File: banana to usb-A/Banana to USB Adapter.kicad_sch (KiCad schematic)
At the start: 11 parts, among them J1 USB_A, J2 Positive, J3 Negative, J4 Data

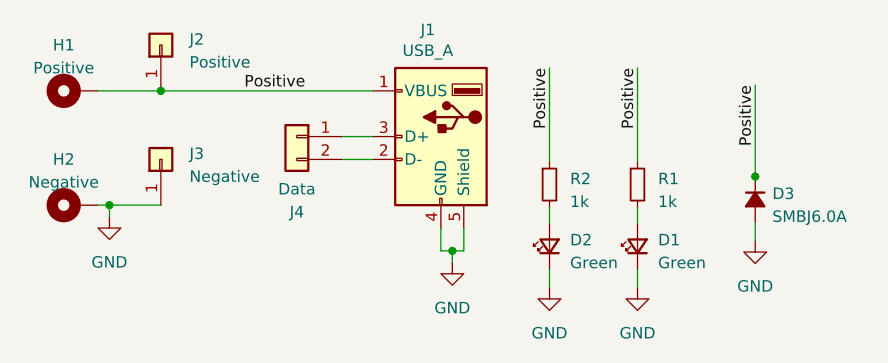
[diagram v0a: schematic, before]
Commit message: No design changes to PCB. Removed extra LED reference in schematic, changed TVS diode to D2, and uploaded PCB.
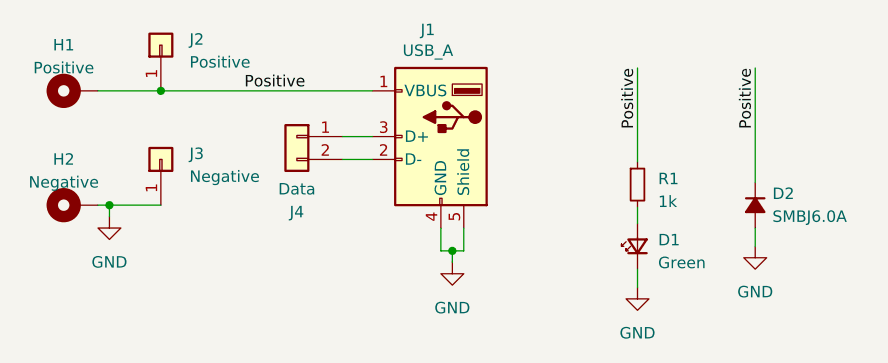
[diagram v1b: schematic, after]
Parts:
- removed D2: Green, LED_SMD:LED_1206_3216Metric_Pad1.42x1.75mm_HandSolder, symbol Device:LED_Small
- removed R2: 1k, Resistor_SMD:R_1206_3216Metric_Pad1.30x1.75mm_HandSolder, symbol Device:R_Small
- renumbered D3 to D2
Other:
- moved on the sheet: D2
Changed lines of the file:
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@@
     (company "baldengineer.com")
   )
-  (junction (at 241.935 86.995) (diameter 0) (color 0 0 0 0)
-  )
   (junction (at 208.28 95.25) (diameter 0) (color 0 0 0 0)
   )
@@
     (stroke (width 0) (type default))
   )
-  (wire (pts (xy 241.935 76.835) (xy 241.935 86.995))
+  (wire (pts (xy 241.935 74.93) (xy 241.935 87.63))
     (stroke (width 0) (type default))
   )
@@
     (stroke (width 0) (type default))
   )
-  (wire (pts (xy 219.075 97.282) (xy 219.075 99.314))
-    (stroke (width 0) (type default))
-  )
   (wire (pts (xy 196.088 85.09) (xy 199.39 85.09))
     (stroke (width 0) (type default))
@@
     (stroke (width 0) (type default))
   )
-  (wire (pts (xy 241.935 86.995) (xy 241.935 87.249))
-    (stroke (width 0) (type default))
-  )
   (wire (pts (xy 175.895 77.47) (xy 199.39 77.47))
     (stroke (width 0) (type default))
   )
-  (wire (pts (xy 241.935 92.075) (xy 241.935 94.107))
+  (wire (pts (xy 241.935 92.71) (xy 241.935 94.742))
     (stroke (width 0) (type default))
   )
@@
   )
   (wire (pts (xy 207.01 95.25) (xy 208.28 95.25))
-    (stroke (width 0) (type default))
-  )
-  (wire (pts (xy 219.075 74.93) (xy 219.075 85.344))
-    (stroke (width 0) (type default))
-  )
-  (wire (pts (xy 219.075 90.424) (xy 219.075 92.202))
     (stroke (width 0) (type default))
   )
@@
     )
   )
-  (label "Positive" (at 219.075 74.93 270) (fields_autoplaced)
+  (label "Positive" (at 241.935 74.93 270) (fields_autoplaced)
     (effects (font (size 1.27 1.27)) (justify right bottom))
-    (property "Netclass" "Power" (at 220.345 74.93 90)
+    (property "Netclass" "Power" (at 243.205 74.93 90)
       (effects (font (size 1.27 1.27) italic) (justify right) hide)
     )
   )
-  (label "Positive" (at 241.935 76.835 270) (fields_autoplaced)
-    (effects (font (size 1.27 1.27)) (justify right bottom))
-    (property "Netclass" "Power" (at 243.205 76.835 90)
-      (effects (font (size 1.27 1.27) italic) (justify right) hide)
-    )
-  )
   (symbol (lib_id "Mechanical:MountingHole_Pad") (at 166.37 90.17 90) (unit 1)
     (in_bom yes) (on_board yes) (dnp no) (fields_autoplaced)
@@
         (path "/b8d30d27-a840-4da1-9b57-1f9fe5fa1469"
           (reference "#PWR02") (unit 1)
-        )
-      )
-    )
-  )
-  (symbol (lib_id "Device:LED_Small") (at 219.075 94.742 90) (unit 1)
-    (in_bom yes) (on_board yes) (dnp no) (fields_autoplaced)
-    (property "Reference" "D2" (at 221.361 94.0435 90)
-      (effects (font (size 1.27 1.27)) (justify right))
-    )
-    (property "Value" "Green" (at 221.361 96.5835 90)
-      (effects (font (size 1.27 1.27)) (justify right))
-    )
-    (property "Footprint" "LED_SMD:LED_1206_3216Metric_Pad1.42x1.75mm_HandSolder" (at 219.075 94.742 90)
-      (effects (font (size 1.27 1.27)) hide)
-    )
-    (property "Datasheet" "~" (at 219.075 94.742 90)
-      (effects (font (size 1.27 1.27)) hide)
-    )
-    (pin "1")
-    (pin "2")
-    (instances
-      (project "Banana to USB Adapter"
-        (path "/b8d30d27-a840-4da1-9b57-1f9fe5fa1469"
-          (reference "D2") (unit 1)
         )
       )
@@
     )
   )
-  (symbol (lib_id "power:GND") (at 219.075 99.314 0) (unit 1)
-    (in_bom yes) (on_board yes) (dnp no) (fields_autoplaced)
-    (property "Reference" "#PWR05" (at 219.075 105.664 0)
-      (effects (font (size 1.27 1.27)) hide)
-    )
-    (property "Value" "GND" (at 219.075 104.394 0)
-      (effects (font (size 1.27 1.27)))
-    )
-    (property "Footprint" "" (at 219.075 99.314 0)
-      (effects (font (size 1.27 1.27)) hide)
-    )
-    (property "Datasheet" "" (at 219.075 99.314 0)
-      (effects (font (size 1.27 1.27)) hide)
-    )
-    (pin "1")
-    (instances
-      (project "Banana to USB Adapter"
-        (path "/b8d30d27-a840-4da1-9b57-1f9fe5fa1469"
-          (reference "#PWR05") (unit 1)
-        )
-      )
-    )
-  )
   (symbol (lib_id "Connector_Generic:Conn_01x01") (at 175.895 85.09 90) (unit 1)
     (in_bom yes) (on_board yes) (dnp no) (fields_autoplaced)
@@
     )
   )
-  (symbol (lib_id "Device:D_Small_Filled") (at 241.935 89.535 270) (unit 1)
-    (in_bom yes) (on_board yes) (dnp no) (fields_autoplaced)
-    (property "Reference" "D3" (at 243.84 88.9 90)
+  (symbol (lib_id "Device:D_Small_Filled") (at 241.935 90.17 270) (unit 1)
+    (in_bom yes) (on_board yes) (dnp no) (fields_autoplaced)
+    (property "Reference" "D2" (at 243.84 88.9 90)
       (effects (font (size 1.27 1.27)) (justify left))
     )
@@
       (effects (font (size 1.27 1.27)) (justify left))
     )
-    (property "Footprint" "Diode_SMD:D_SMA-SMB_Universal_Handsoldering" (at 241.935 89.535 90)
-      (effects (font (size 1.27 1.27)) hide)
-    )
-    (property "Datasheet" "https://www.farnell.com/datasheets/1874873.pdf" (at 241.935 89.535 90)
-      (effects (font (size 1.27 1.27)) hide)
-    )
-    (property "Sim.Device" "D" (at 241.935 89.535 0)
-      (effects (font (size 1.27 1.27)) hide)
-    )
-    (property "Sim.Pins" "1=K 2=A" (at 241.935 89.535 0)
+    (property "Footprint" "Diode_SMD:D_SMA-SMB_Universal_Handsoldering" (at 241.935 90.17 90)
+      (effects (font (size 1.27 1.27)) hide)
+    )
+    (property "Datasheet" "https://www.farnell.com/datasheets/1874873.pdf" (at 241.935 90.17 90)
+      (effects (font (size 1.27 1.27)) hide)
+    )
+    (property "Sim.Device" "D" (at 241.935 90.17 0)
+      (effects (font (size 1.27 1.27)) hide)
+    )
+    (property "Sim.Pins" "1=K 2=A" (at 241.935 90.17 0)
       (effects (font (size 1.27 1.27)) hide)
     )
@@
       (project "Banana to USB Adapter"
         (path "/b8d30d27-a840-4da1-9b57-1f9fe5fa1469"
-          (reference "D3") (unit 1)
+          (reference "D2") (unit 1)
         )
       )
@@
     )
   )
-  (symbol (lib_id "power:GND") (at 241.935 94.107 0) (unit 1)
-    (in_bom yes) (on_board yes) (dnp no) (fields_autoplaced)
-    (property "Reference" "#PWR04" (at 241.935 100.457 0)
-      (effects (font (size 1.27 1.27)) hide)
-    )
-    (property "Value" "GND" (at 241.935 99.187 0)
-      (effects (font (size 1.27 1.27)))
-    )
-    (property "Footprint" "" (at 241.935 94.107 0)
-      (effects (font (size 1.27 1.27)) hide)
-    )
-    (property "Datasheet" "" (at 241.935 94.107 0)
+  (symbol (lib_id "power:GND") (at 241.935 94.742 0) (unit 1)
+    (in_bom yes) (on_board yes) (dnp no) (fields_autoplaced)
+    (property "Reference" "#PWR04" (at 241.935 101.092 0)
+      (effects (font (size 1.27 1.27)) hide)
+    )
+    (property "Value" "GND" (at 241.935 99.822 0)
+      (effects (font (size 1.27 1.27)))
+    )
+    (property "Footprint" "" (at 241.935 94.742 0)
+      (effects (font (size 1.27 1.27)) hide)
+    )
+    (property "Datasheet" "" (at 241.935 94.742 0)
       (effects (font (size 1.27 1.27)) hide)
     )
@@
         )
       )
-    )
-  )
-  (symbol (lib_id "Device:R_Small") (at 219.075 87.884 0) (unit 1)
-    (in_bom yes) (on_board yes) (dnp no) (fields_autoplaced)
-    (property "Reference" "R2" (at 221.361 87.249 0)
-      (effects (font (size 1.27 1.27)) (justify left))
-    )
-    (property "Value" "1k" (at 221.361 89.789 0)
-      (effects (font (size 1.27 1.27)) (justify left))
-    )
-    (property "Footprint" "Resistor_SMD:R_1206_3216Metric_Pad1.30x1.75mm_HandSolder" (at 219.075 87.884 0)
-      (effects (font (size 1.27 1.27)) hide)
-    )
-    (property "Datasheet" "~" (at 219.075 87.884 0)
-      (effects (font (size 1.27 1.27)) hide)
-    )
-    (pin "1")
-    (pin "2")
-    (instances
-      (project "Banana to USB Adapter"
-        (path "/b8d30d27-a840-4da1-9b57-1f9fe5fa1469"
-          (reference "R2") (unit 1)
-        )
-      )
